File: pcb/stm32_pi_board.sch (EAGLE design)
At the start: 67 parts, among them IC1 LD1117, IC2 ESP-11, IC3 LD1117, IC4 STM32F405RG, IC5 STF203-22, Q1 BSH205, Q2 N2004, Q5 BSH205, Q6 N2004, X1 PJ-043-SMT, X2 DM3AT, X3 XM7D-0512

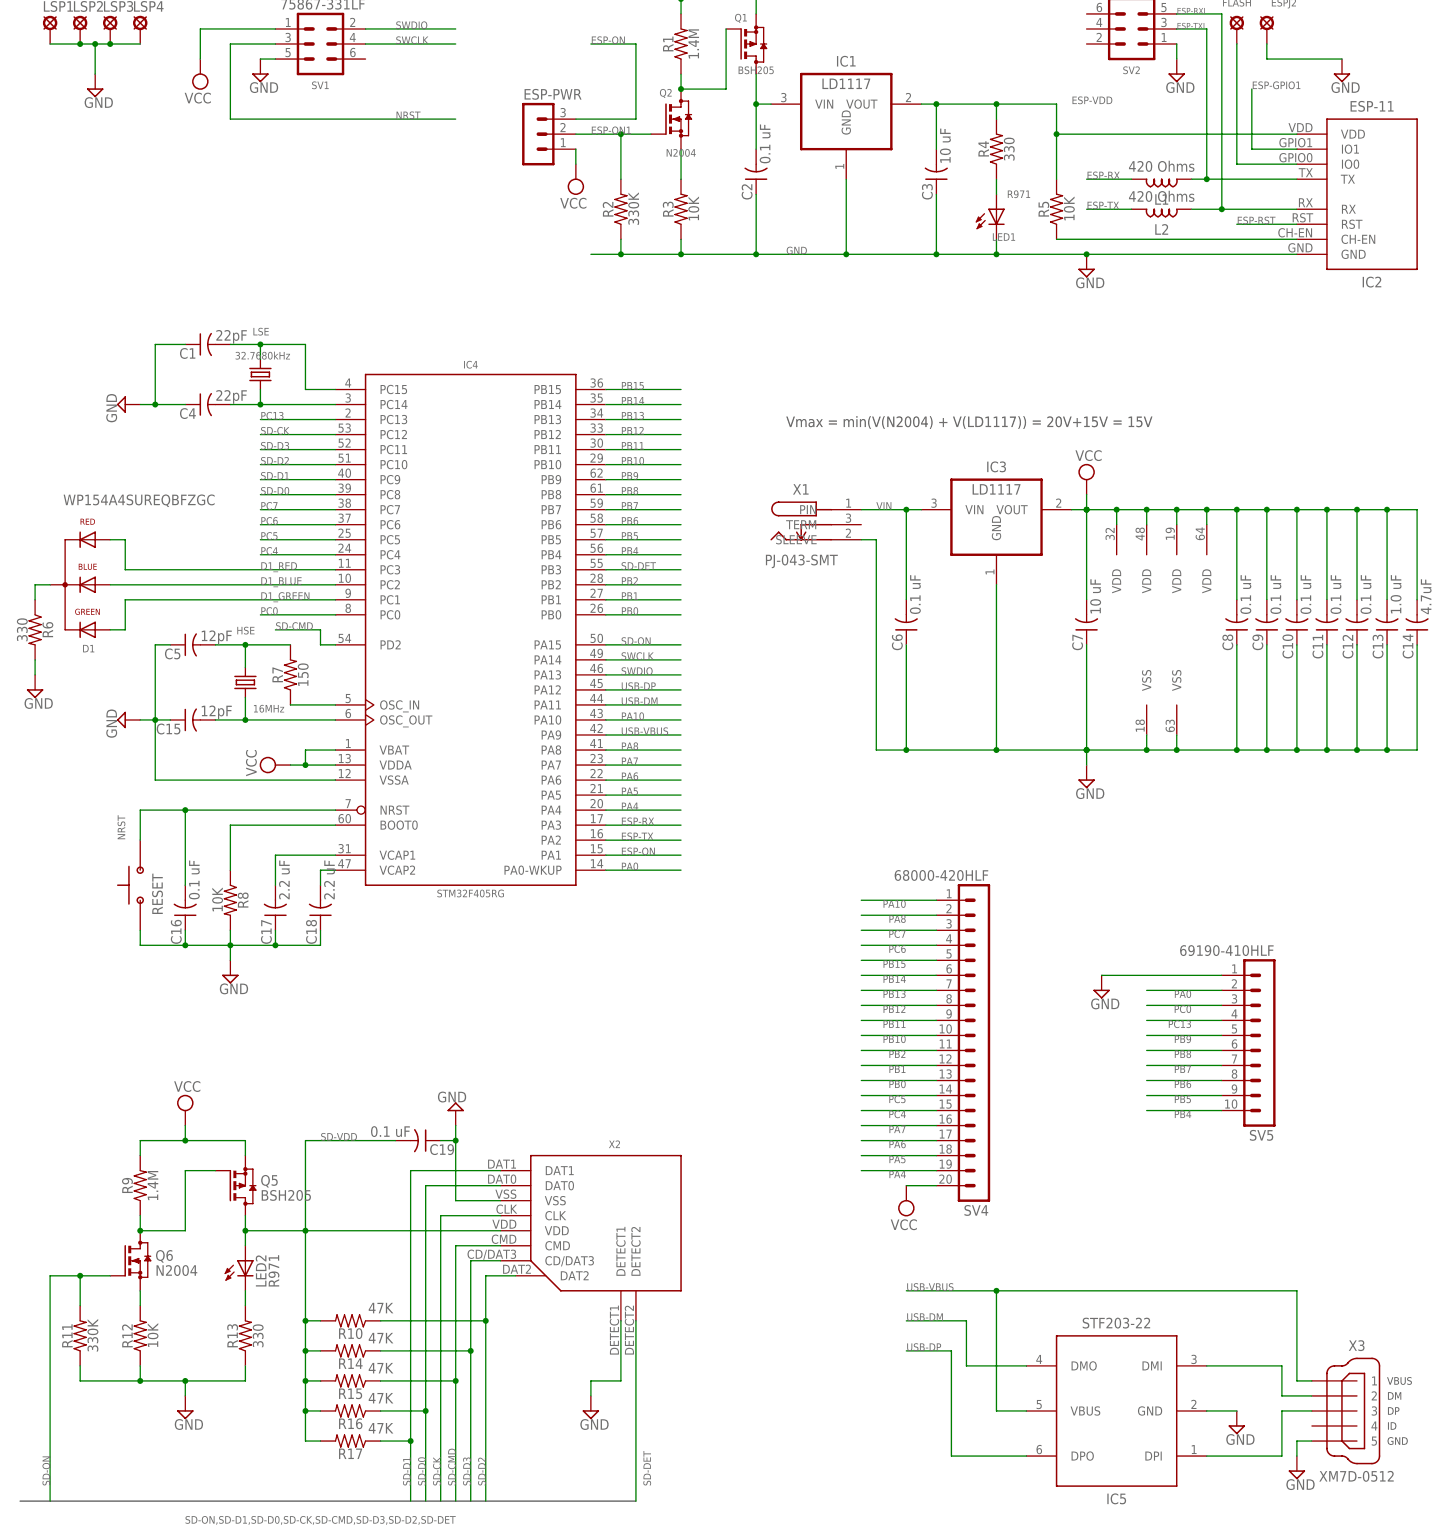
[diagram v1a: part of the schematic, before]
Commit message: Fixed minor layout bugs
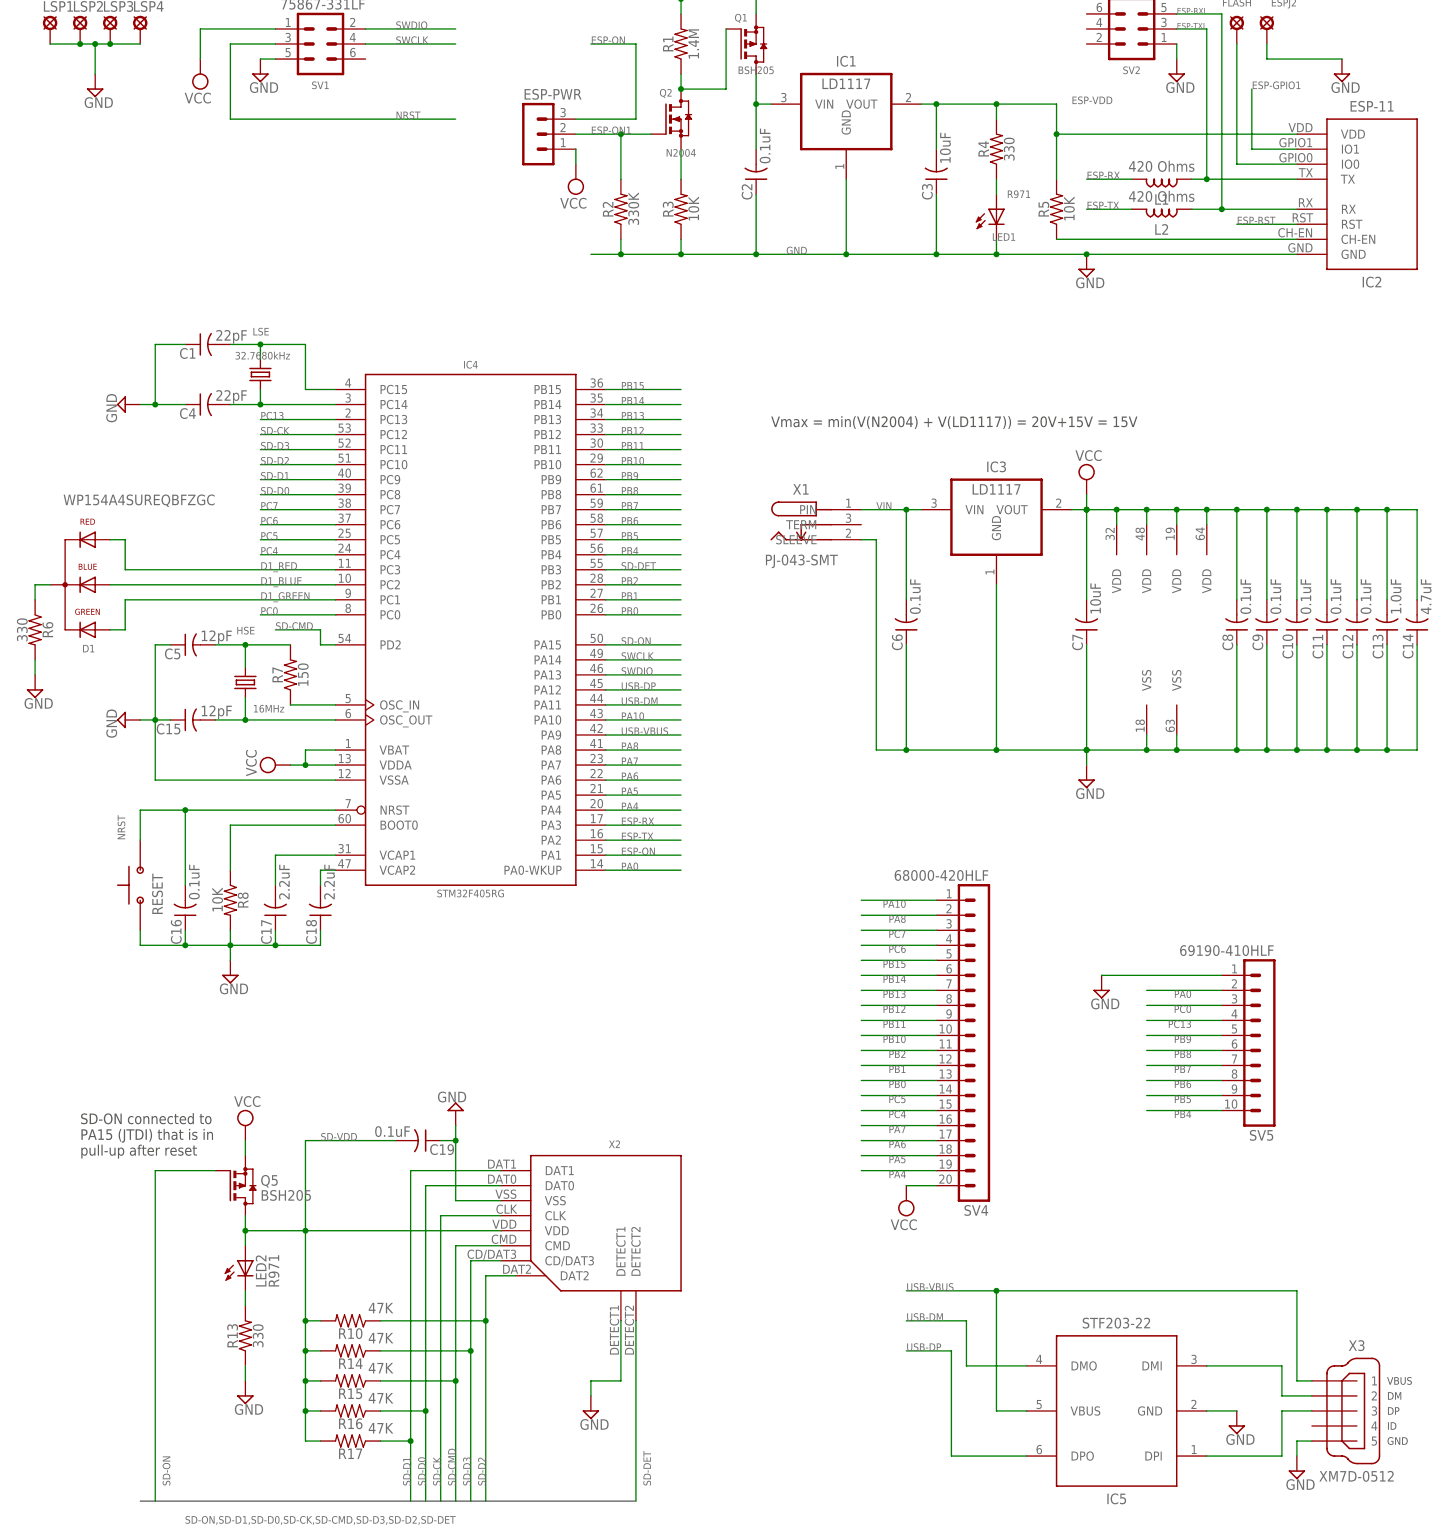
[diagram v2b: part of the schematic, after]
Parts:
- removed Q6: N2004, MyComponents:N2004
- removed R11: 330K, MyComponents:R-US0805
- removed R12: 10K, MyComponents:R-US0805
- removed R9: 1.4M, MyComponents:R-US0805
- C10, C11, C12, C16, C19, C2, C6, C8, C9: value 0.1 uF -> 0.1uF
- C13: value 1.0 uF -> 1.0uF
- C17, C18: value 2.2 uF -> 2.2uF
- C3, C7: value 10 uF -> 10uF
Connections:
- removed net D_VG: Q5.G, Q6.D, R9.1
- removed net N$136: Q6.S, R12.2
- net GND: no longer R11.1, R12.1
- net SD-ON: now also Q5.G; no longer Q6.G, R11.2
- net VDD: no longer R9.2
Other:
- note added: "SD-ON connected to PA15 (JTDI) that is in pull-up after reset"
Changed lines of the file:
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@@
 <part name="IC2" library="MyComponents" deviceset="ESP-11" device=""/>
 <part name="IC3" library="MyComponents" deviceset="REG1117" device="" value="LD1117"/>
-<part name="C6" library="MyComponents" deviceset="C-US" device="0805" value="0.1 uF"/>
-<part name="C7" library="MyComponents" deviceset="C-US" device="0805" value="10 uF"/>
+<part name="C6" library="MyComponents" deviceset="C-US" device="0805" value="0.1uF"/>
+<part name="C7" library="MyComponents" deviceset="C-US" device="0805" value="10uF"/>
 <part name="SUPPLY31" library="supply2" deviceset="GND" device=""/>
 <part name="SUPPLY34" library="supply2" deviceset="VCC" device=""/>
 <part name="IC4" library="stm32" deviceset="STM32F405R*T" device="" technology="G" value="STM32F405RG"/>
-<part name="C8" library="MyComponents" deviceset="C-US" device="0805" value="0.1 uF"/>
-<part name="C9" library="MyComponents" deviceset="C-US" device="0805" value="0.1 uF"/>
-<part name="C10" library="MyComponents" deviceset="C-US" device="0805" value="0.1 uF"/>
+<part name="C8" library="MyComponents" deviceset="C-US" device="0805" value="0.1uF"/>
+<part name="C9" library="MyComponents" deviceset="C-US" device="0805" value="0.1uF"/>
+<part name="C10" library="MyComponents" deviceset="C-US" device="0805" value="0.1uF"/>
 <part name="C14" library="MyComponents" deviceset="C-US" device="0805" value="4.7uF"/>
-<part name="C16" library="MyComponents" deviceset="C-US" device="0805" value="0.1 uF"/>
+<part name="C16" library="MyComponents" deviceset="C-US" device="0805" value="0.1uF"/>
 <part name="R8" library="MyComponents" deviceset="R-US" device="0805" value="10K"/>
 <part name="RESET" library="MyComponents" deviceset="BUTTON-FSM14JRT" device=""/>
@@
 <part name="SUPPLY36" library="supply2" deviceset="GND" device=""/>
 <part name="SUPPLY30" library="supply2" deviceset="VCC" device=""/>
-<part name="C18" library="MyComponents" deviceset="C-US" device="0805" value="2.2 uF"/>
-<part name="C17" library="MyComponents" deviceset="C-US" device="0805" value="2.2 uF"/>
+<part name="C18" library="MyComponents" deviceset="C-US" device="0805" value="2.2uF"/>
+<part name="C17" library="MyComponents" deviceset="C-US" device="0805" value="2.2uF"/>
 <part name="SUPPLY29" library="supply2" deviceset="GND" device=""/>
 <part name="SUPPLY32" library="supply2" deviceset="GND" device=""/>
-<part name="C11" library="MyComponents" deviceset="C-US" device="0805" value="0.1 uF"/>
-<part name="C13" library="MyComponents" deviceset="C-US" device="0805" value="1.0 uF"/>
+<part name="C11" library="MyComponents" deviceset="C-US" device="0805" value="0.1uF"/>
+<part name="C13" library="MyComponents" deviceset="C-US" device="0805" value="1.0uF"/>
 <part name="X2" library="MyComponents" deviceset="MICRO-SD-DM3AT" device="" value="DM3AT"/>
-<part name="C19" library="MyComponents" deviceset="C-US" device="0805" value="0.1 uF"/>
+<part name="C19" library="MyComponents" deviceset="C-US" device="0805" value="0.1uF"/>
 <part name="R13" library="MyComponents" deviceset="R-US" device="0805" value="330"/>
 <part name="LED2" library="led" deviceset="LED" device="CHIP-LED0805" value="R971"/>
-<part name="R12" library="MyComponents" deviceset="R-US" device="0805" value="10K"/>
-<part name="R9" library="MyComponents" deviceset="R-US" device="0805" value="1.4M"/>
-<part name="Q6" library="MyComponents" deviceset="N2004" device="" value="N2004"/>
-<part name="R11" library="MyComponents" deviceset="R-US" device="0805" value="330K"/>
 <part name="Q5" library="MyComponents" deviceset="BSH205G2R" device="" value="BSH205"/>
 <part name="SUPPLY27" library="supply2" deviceset="VCC" device=""/>
@@
 <part name="SUPPLY24" library="supply2" deviceset="GND" device=""/>
 <part name="SUPPLY23" library="supply2" deviceset="GND" device=""/>
-<part name="C12" library="MyComponents" deviceset="C-US" device="0805" value="0.1 uF"/>
+<part name="C12" library="MyComponents" deviceset="C-US" device="0805" value="0.1uF"/>
 <part name="SV4" library="MyComponents" deviceset="MA20-1" device="NO-PL" value="68000-420HLF"/>
 <part name="SV5" library="MyComponents" deviceset="MA10-1" device="NO-PL" value="69190-410HLF"/>
@@
 <part name="Q1" library="MyComponents" deviceset="BSH205G2R" device="" value="BSH205"/>
 <part name="IC1" library="MyComponents" deviceset="REG1117" device="" value="LD1117"/>
-<part name="C2" library="MyComponents" deviceset="C-US" device="0805" value="0.1 uF"/>
-<part name="C3" library="MyComponents" deviceset="C-US" device="0805" value="10 uF"/>
+<part name="C2" library="MyComponents" deviceset="C-US" device="0805" value="0.1uF"/>
+<part name="C3" library="MyComponents" deviceset="C-US" device="0805" value="10uF"/>
 <part name="R5" library="MyComponents" deviceset="R-US" device="0805" value="10K"/>
 <part name="R10" library="MyComponents" deviceset="R-US" device="0805" value="47K"/>
@@
 <description>Centrale and sensor</description>
 <plain>
-<text x="165.1" y="181.61" size="1.778" layer="97">Vmax = min(V(N2004) + V(LD1117)) = 20V+15V = 15V</text>
+<text x="162.56" y="181.61" size="1.778" layer="97">Vmax = min(V(N2004) + V(LD1117)) = 20V+15V = 15V</text>
+<text x="45.72" y="58.42" size="1.778" layer="97">SD-ON connected to
+PA15 (JTDI) that is in
+pull-up after reset</text>
 </plain>
 <instances>
@@
 <instance part="R13" gate="G$1" x="73.66" y="27.94" rot="R90"/>
 <instance part="LED2" gate="G$1" x="73.66" y="40.64"/>
-<instance part="R12" gate="G$1" x="55.88" y="27.94" rot="R90"/>
-<instance part="R9" gate="G$1" x="55.88" y="53.34" rot="R90"/>
-<instance part="Q6" gate="G$1" x="55.88" y="40.64"/>
-<instance part="R11" gate="G$1" x="45.72" y="27.94" rot="R90"/>
 <instance part="Q5" gate="G$1" x="73.66" y="53.34"/>
-<instance part="SUPPLY27" gate="G$1" x="63.5" y="66.04"/>
-<instance part="SUPPLY25" gate="GND" x="63.5" y="15.24"/>
+<instance part="SUPPLY27" gate="G$1" x="73.66" y="63.5"/>
+<instance part="SUPPLY25" gate="GND" x="73.66" y="17.78"/>
 <instance part="SUPPLY28" gate="GND" x="109.22" y="66.04" rot="R180"/>
 <instance part="SUPPLY26" gate="GND" x="132.08" y="15.24"/>
@@
 <bus name="SD-ON,SD-D1,SD-D0,SD-CK,SD-CMD,SD-D3,SD-D2,SD-DET">
 <segment>
-<wire x1="35.56" y1="0" x2="139.7" y2="0" width="0.762" layer="92"/>
+<wire x1="55.88" y1="0" x2="139.7" y2="0" width="0.762" layer="92"/>
 <label x="109.22" y="-2.54" size="1.27" layer="95" rot="R180"/>
 </segment>
@@
 </segment>
 <segment>
-<pinref part="R11" gate="G$1" pin="1"/>
-<wire x1="45.72" y1="22.86" x2="45.72" y2="20.32" width="0.1524" layer="91"/>
 <pinref part="R13" gate="G$1" pin="1"/>
-<wire x1="45.72" y1="20.32" x2="55.88" y2="20.32" width="0.1524" layer="91"/>
-<wire x1="55.88" y1="20.32" x2="63.5" y2="20.32" width="0.1524" layer="91"/>
-<wire x1="63.5" y1="20.32" x2="73.66" y2="20.32" width="0.1524" layer="91"/>
+<pinref part="SUPPLY25" gate="GND" pin="GND"/>
 <wire x1="73.66" y1="20.32" x2="73.66" y2="22.86" width="0.1524" layer="91"/>
-<pinref part="SUPPLY25" gate="GND" pin="GND"/>
-<wire x1="63.5" y1="17.78" x2="63.5" y2="20.32" width="0.1524" layer="91"/>
-<junction x="63.5" y="20.32"/>
-<pinref part="R12" gate="G$1" pin="1"/>
-<wire x1="55.88" y1="22.86" x2="55.88" y2="20.32" width="0.1524" layer="91"/>
-<junction x="55.88" y="20.32"/>
 </segment>
 <segment>
@@
 </segment>
 <segment>
-<pinref part="R9" gate="G$1" pin="2"/>
-<wire x1="55.88" y1="58.42" x2="55.88" y2="60.96" width="0.1524" layer="91"/>
 <pinref part="Q5" gate="G$1" pin="S"/>
-<wire x1="55.88" y1="60.96" x2="63.5" y2="60.96" width="0.1524" layer="91"/>
-<wire x1="63.5" y1="60.96" x2="73.66" y2="60.96" width="0.1524" layer="91"/>
+<pinref part="SUPPLY27" gate="G$1" pin="VCC"/>
 <wire x1="73.66" y1="60.96" x2="73.66" y2="58.42" width="0.1524" layer="91"/>
-<pinref part="SUPPLY27" gate="G$1" pin="VCC"/>
-<wire x1="63.5" y1="63.5" x2="63.5" y2="60.96" width="0.1524" layer="91"/>
-<junction x="63.5" y="60.96"/>
 </segment>
 <segment>
@@
 </segment>
 </net>
-<net name="N$136" class="0">
-<segment>
-<pinref part="R12" gate="G$1" pin="2"/>
-<pinref part="Q6" gate="G$1" pin="S"/>
-<wire x1="55.88" y1="33.02" x2="55.88" y2="35.56" width="0.1524" layer="91"/>
-</segment>
-</net>
 <net name="N$120" class="0">
 <segment>
@@
 <pinref part="R13" gate="G$1" pin="2"/>
 <wire x1="73.66" y1="35.56" x2="73.66" y2="33.02" width="0.1524" layer="91"/>
-</segment>
-</net>
-<net name="D_VG" class="0">
-<segment>
-<pinref part="Q6" gate="G$1" pin="D"/>
-<pinref part="R9" gate="G$1" pin="1"/>
-<wire x1="55.88" y1="48.26" x2="55.88" y2="45.72" width="0.1524" layer="91"/>
-<wire x1="55.88" y1="45.72" x2="63.5" y2="45.72" width="0.1524" layer="91"/>
-<junction x="55.88" y="45.72"/>
-<wire x1="63.5" y1="45.72" x2="63.5" y2="55.88" width="0.1524" layer="91"/>
-<pinref part="Q5" gate="G$1" pin="G"/>
-<wire x1="63.5" y1="55.88" x2="68.58" y2="55.88" width="0.1524" layer="91"/>
 </segment>
 </net>
@@
 <net name="SD-ON" class="0">
 <segment>
-<wire x1="40.64" y1="0" x2="40.64" y2="38.1" width="0.1524" layer="91"/>
-<pinref part="Q6" gate="G$1" pin="G"/>
-<pinref part="R11" gate="G$1" pin="2"/>
-<wire x1="50.8" y1="38.1" x2="45.72" y2="38.1" width="0.1524" layer="91"/>
-<wire x1="45.72" y1="38.1" x2="45.72" y2="33.02" width="0.1524" layer="91"/>
-<wire x1="40.64" y1="38.1" x2="45.72" y2="38.1" width="0.1524" layer="91"/>
-<junction x="45.72" y="38.1"/>
-<label x="40.64" y="2.54" size="1.27" layer="95" rot="R90"/>
+<wire x1="58.42" y1="0" x2="58.42" y2="55.88" width="0.1524" layer="91"/>
+<label x="60.96" y="2.54" size="1.27" layer="95" rot="R90"/>
+<pinref part="Q5" gate="G$1" pin="G"/>
+<wire x1="58.42" y1="55.88" x2="68.58" y2="55.88" width="0.1524" layer="91"/>
 </segment>
 <segment>
@@
 </schematic>
 </drawing>
+<compatibility>
+<note version="6.3" minversion="6.2.2" severity="warning">
+Since Version 6.2.2 text objects can contain more than one line,
+which will not be processed correctly with this version.
+</note>
+</compatibility>
 </eagle>
